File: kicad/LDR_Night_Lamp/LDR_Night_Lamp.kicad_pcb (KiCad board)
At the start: 2 copper layers, 68.5 x 38 mm, 6 parts, among them Q1 BC547

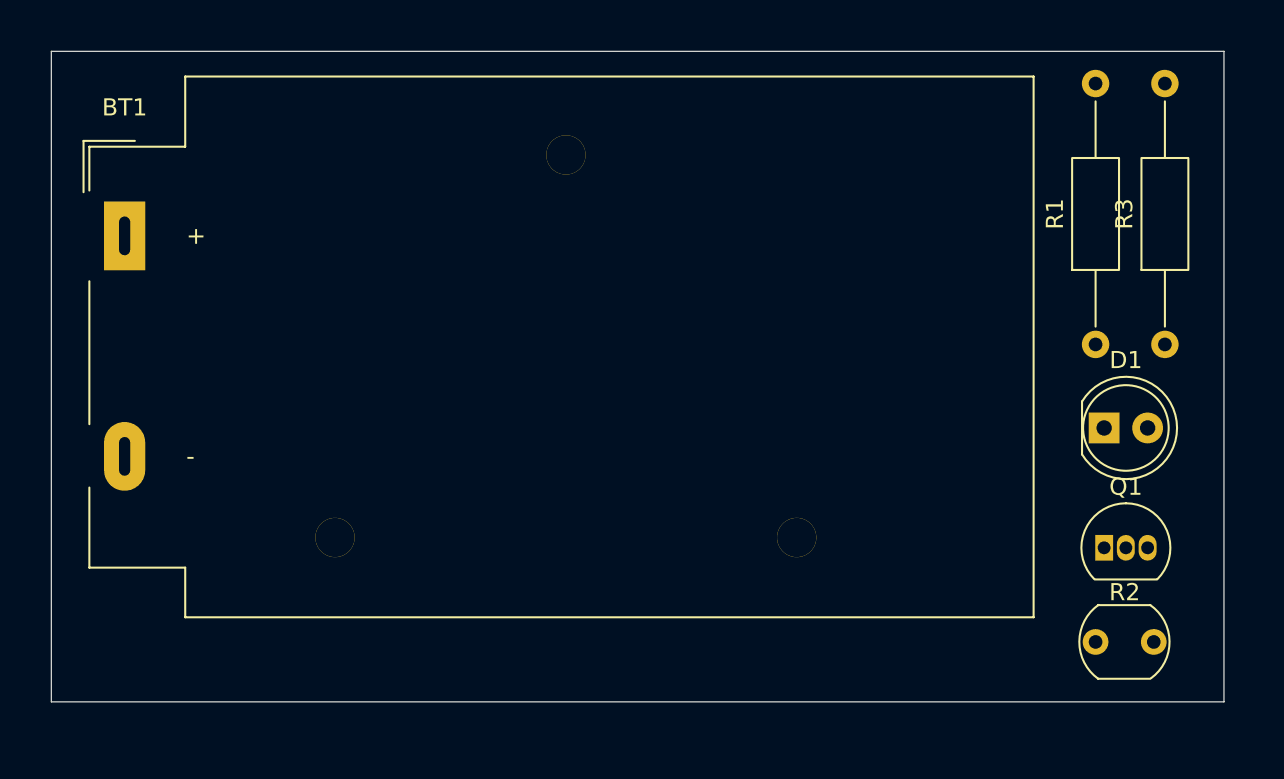
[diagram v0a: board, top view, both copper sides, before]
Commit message: feat: completed PCB routing and added copper pours
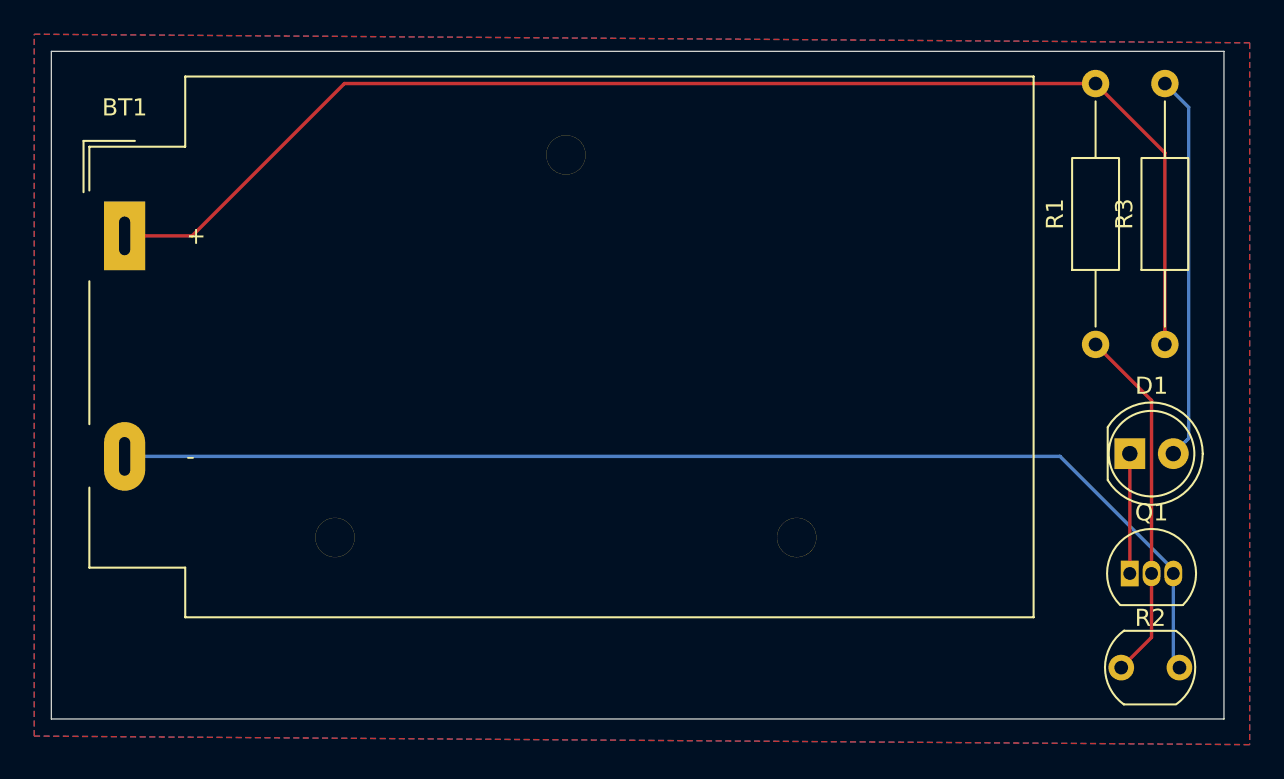
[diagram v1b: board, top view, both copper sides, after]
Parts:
- moved D1 2.12 mm to (164.0, 74.0)
- moved Q1 2.12 mm to (164.0, 81.0)
- moved R2 2.12 mm to (163.5, 86.5)
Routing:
- net Net-(BT1-+): track 0.00 -> 77.3 mm
- net Net-(BT1--): track 0.00 -> 69.9 mm
- net Net-(D1-A): track 0.00 -> 22.6 mm
- net Net-(Q1-B): track 0.00 -> 21.0 mm
- net Net-(D1-K): track 0.00 -> 7.00 mm
- added copper zone on B.Cu, net Net-(BT1--)
- added copper zone on F.Cu, net Net-(BT1--)
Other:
- board size 68.5 x 38 mm -> 68.5 x 39 mm
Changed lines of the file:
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@@
 	(footprint "OptoDevice:R_LDR_5.1x4.3mm_P3.4mm_Vertical"
 		(layer "F.Cu")
-		(at 162 85)
+		(at 163.5 86.5)
 		(descr "Resistor, LDR 5.1x3.4mm, see http://yourduino.com/docs/Photoresistor-5516-datasheet.pdf")
 		(tags "Resistor LDR5.1x3.4mm")
@@
 	(footprint "LED_THT:LED_D5.0mm"
 		(layer "F.Cu")
-		(at 162.5 72.5)
+		(at 164 74)
 		(descr "LED, diameter 5.0mm, 2 pins, http://cdn-reichelt.de/documents/datenblatt/A500/LL-504BC2E-009.pdf, generated by kicad-footprint-generator")
 		(tags "LED")
@@
 	(footprint "Package_TO_SOT_THT:TO-92_Inline"
 		(layer "F.Cu")
-		(at 162.5 79.5)
+		(at 164 81)
 		(descr "TO-92 leads in-line, narrow, oval pads, drill 0.75mm (see NXP sot054_po.pdf)")
 		(tags "to-92 sc-43 sc-43a sot54 PA33 transistor")
@@
 	(gr_rect
 		(start 101 50.5)
-		(end 169.5 88.5)
+		(end 169.5 89.5)
 		(stroke
 			(width 0.05)
@@
 		(layer "Edge.Cuts")
 	)
+	(segment
+		(start 159.925 74.16)
+		(end 105.28 74.16)
+		(width 0.2)
+		(layer "B.Cu")
+		(net 1)
+	)
+	(segment
+		(start 166.54 81)
+		(end 166.54 80.775)
+		(width 0.2)
+		(layer "B.Cu")
+		(net 1)
+	)
+	(segment
+		(start 166.54 81)
+		(end 166.54 86.14)
+		(width 0.2)
+		(layer "B.Cu")
+		(net 1)
+	)
+	(segment
+		(start 166.54 86.14)
+		(end 166.9 86.5)
+		(width 0.2)
+		(layer "B.Cu")
+		(net 1)
+	)
+	(segment
+		(start 166.54 80.775)
+		(end 159.925 74.16)
+		(width 0.2)
+		(layer "B.Cu")
+		(net 1)
+	)
+	(segment
+		(start 109.22 61.28)
+		(end 105.28 61.28)
+		(width 0.2)
+		(layer "F.Cu")
+		(net 2)
+	)
+	(segment
+		(start 118.12 52.38)
+		(end 109.22 61.28)
+		(width 0.2)
+		(layer "F.Cu")
+		(net 2)
+	)
+	(segment
+		(start 162 52.38)
+		(end 118.12 52.38)
+		(width 0.2)
+		(layer "F.Cu")
+		(net 2)
+	)
+	(segment
+		(start 166.05 67.62)
+		(end 166.05 56.43)
+		(width 0.2)
+		(layer "F.Cu")
+		(net 2)
+	)
+	(segment
+		(start 166.05 56.43)
+		(end 162 52.38)
+		(width 0.2)
+		(layer "F.Cu")
+		(net 2)
+	)
+	(segment
+		(start 164 81)
+		(end 164 74)
+		(width 0.2)
+		(layer "F.Cu")
+		(net 3)
+	)
+	(segment
+		(start 167.44 73.1)
+		(end 167.44 53.77)
+		(width 0.2)
+		(layer "B.Cu")
+		(net 4)
+	)
+	(segment
+		(start 167.44 53.77)
+		(end 166.05 52.38)
+		(width 0.2)
+		(layer "B.Cu")
+		(net 4)
+	)
+	(segment
+		(start 166.54 74)
+		(end 167.44 73.1)
+		(width 0.2)
+		(layer "B.Cu")
+		(net 4)
+	)
+	(segment
+		(start 165.27 70.89)
+		(end 165.27 81)
+		(width 0.2)
+		(layer "F.Cu")
+		(net 5)
+	)
+	(segment
+		(start 162 67.62)
+		(end 165.27 70.89)
+		(width 0.2)
+		(layer "F.Cu")
+		(net 5)
+	)
+	(segment
+		(start 165.27 81)
+		(end 165.27 84.73)
+		(width 0.2)
+		(layer "F.Cu")
+		(net 5)
+	)
+	(segment
+		(start 165.27 84.73)
+		(end 163.5 86.5)
+		(width 0.2)
+		(layer "F.Cu")
+		(net 5)
+	)
+	(zone
+		(net 1)
+		(net_name "Net-(BT1--)")
+		(layers "F.Cu" "B.Cu")
+		(hatch edge 0.5)
+		(connect_pads
+			(clearance 0.5)
+		)
+		(min_thickness 0.25)
+		(filled_areas_thickness no)
+		(fill
+			(thermal_gap 0.5)
+			(thermal_bridge_width 0.5)
+		)
+		(polygon
+			(pts
+				(xy 100 49.5) (xy 171 50) (xy 171 91) (xy 100 90.5)
+			)
+		)
+	)
 	(embedded_fonts no)
